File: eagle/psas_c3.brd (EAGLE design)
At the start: 100 x 80 mm, 56 parts, among them IC1 CP2102, U1 MIC5219 3.3V, Y1 32MHz

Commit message: GPIO connection
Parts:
- added TP6: (no value), psas_c3:1X01_ROUND
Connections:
- new net DIO2: JP6.17, TP6.1, U$1.51
- new net PTD4: JP6.16, JP7.1
- new net PTE2: JP6.5, U$1.49
- net PTE18: now also U$1.7
- net PTE19: now also U$1.8
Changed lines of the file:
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@@
 <element name="JP6" library="pinhead" package="2X09/90" value="" x="-54.61" y="-82.55"/>
 <element name="JP7" library="SparkFun-v5" package="1X02" value="" x="-67.31" y="-93.98"/>
+<element name="TP6" library="psas_c3" package="1X01_ROUND" value="" x="-72.39" y="-91.44">
+<attribute name="BOM" value="EXCLUDE" x="-72.39" y="-91.44" size="1.778" layer="27" display="off"/>
+</element>
 </elements>
 <signals>
@@
 <wire x1="-34.94" y1="22.995" x2="-56.91" y2="-20.82" width="0" layer="19" extent="1-1"/>
 </signal>
-<signal name="N$32">
-<contactref element="IC1" pad="24"/>
-<contactref element="U$1" pad="29"/>
-<wire x1="-20.405" y1="26.11" x2="-54.11" y2="-18.02" width="0" layer="19" extent="1-1"/>
-</signal>
-<signal name="N$33">
-<contactref element="IC1" pad="23"/>
-<contactref element="U$1" pad="28"/>
-<wire x1="-20.88" y1="26.585" x2="-53.61" y2="-18.02" width="0" layer="19" extent="1-1"/>
-</signal>
 <signal name="N$34">
 <contactref element="C20" pad="1"/>
@@
 <signal name="PTE18">
 <contactref element="JP6" pad="10"/>
+<contactref element="U$1" pad="7"/>
+<wire x1="-27.855" y1="22.61" x2="-54.61" y2="-86.36" width="0" layer="19" extent="1-1"/>
 </signal>
 <signal name="PTE17">
@@
 <signal name="PTE19">
 <contactref element="JP6" pad="11"/>
+<contactref element="U$1" pad="8"/>
+<wire x1="-27.855" y1="23.11" x2="-52.07" y2="-88.9" width="0" layer="19" extent="1-1"/>
+</signal>
+<signal name="PTE2">
+<contactref element="U$1" pad="49"/>
+<contactref element="JP6" pad="5"/>
+<wire x1="-23.88" y1="19.135" x2="-59.69" y2="-88.9" width="0" layer="19" extent="1-1"/>
+</signal>
+<signal name="DIO2">
+<contactref element="U$1" pad="51"/>
+<contactref element="JP6" pad="17"/>
+<contactref element="TP6" pad="1"/>
+<wire x1="-44.45" y1="-88.9" x2="-72.39" y2="-91.44" width="0" layer="19" extent="1-1"/>
+<wire x1="-24.88" y1="19.135" x2="-44.45" y2="-88.9" width="0" layer="19" extent="1-1"/>
+</signal>
+<signal name="PTD4">
+<contactref element="JP6" pad="16"/>
+<contactref element="JP7" pad="1"/>
+<wire x1="-46.99" y1="-86.36" x2="-67.31" y2="-93.98" width="0" layer="19" extent="1-1"/>
+</signal>
+<signal name="N$39">
+<contactref element="U$1" pad="29"/>
+<contactref element="IC1" pad="24"/>
+<wire x1="-20.405" y1="26.11" x2="-54.11" y2="-18.02" width="0" layer="19" extent="1-1"/>
+</signal>
+<signal name="N$32">
+<contactref element="U$1" pad="28"/>
+<contactref element="IC1" pad="23"/>
+<wire x1="-20.88" y1="26.585" x2="-53.61" y2="-18.02" width="0" layer="19" extent="1-1"/>
 </signal>
 </signals>

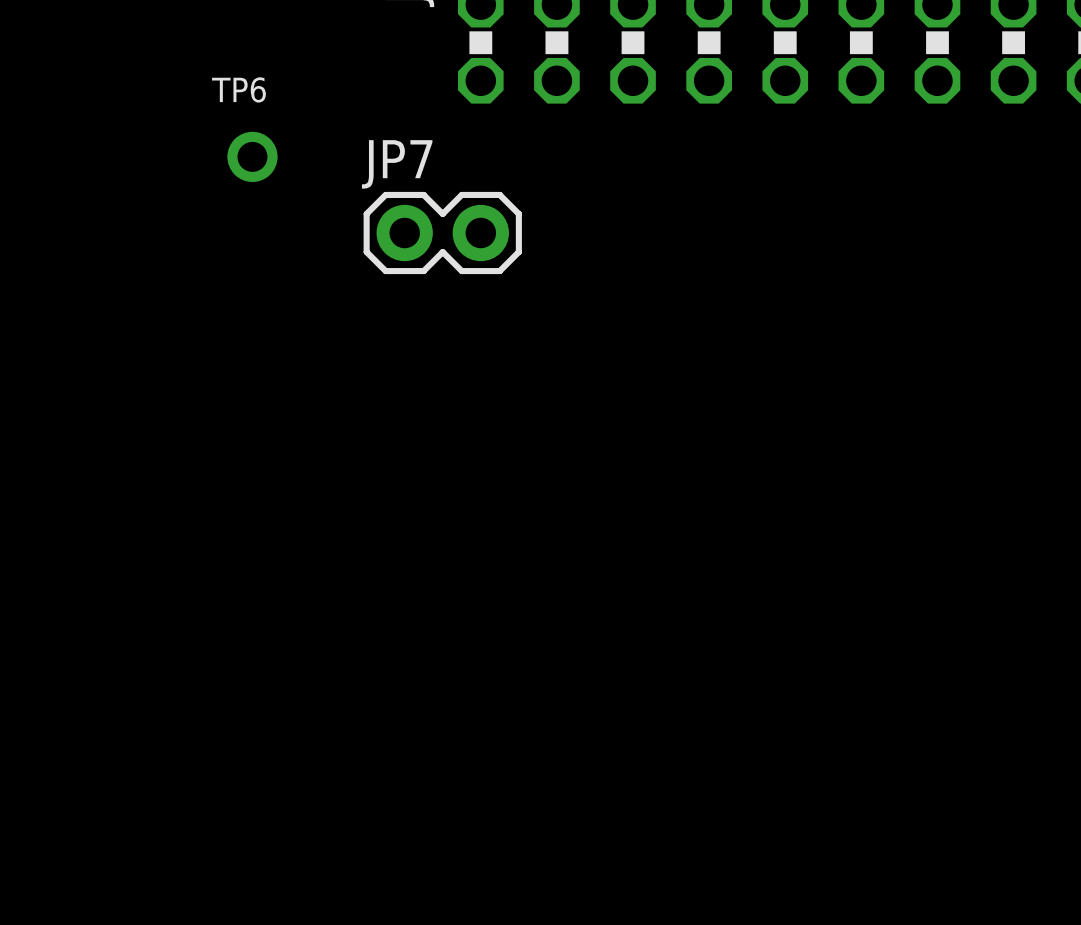
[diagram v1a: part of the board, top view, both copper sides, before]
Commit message: Added GPIO 2x9 pinheader
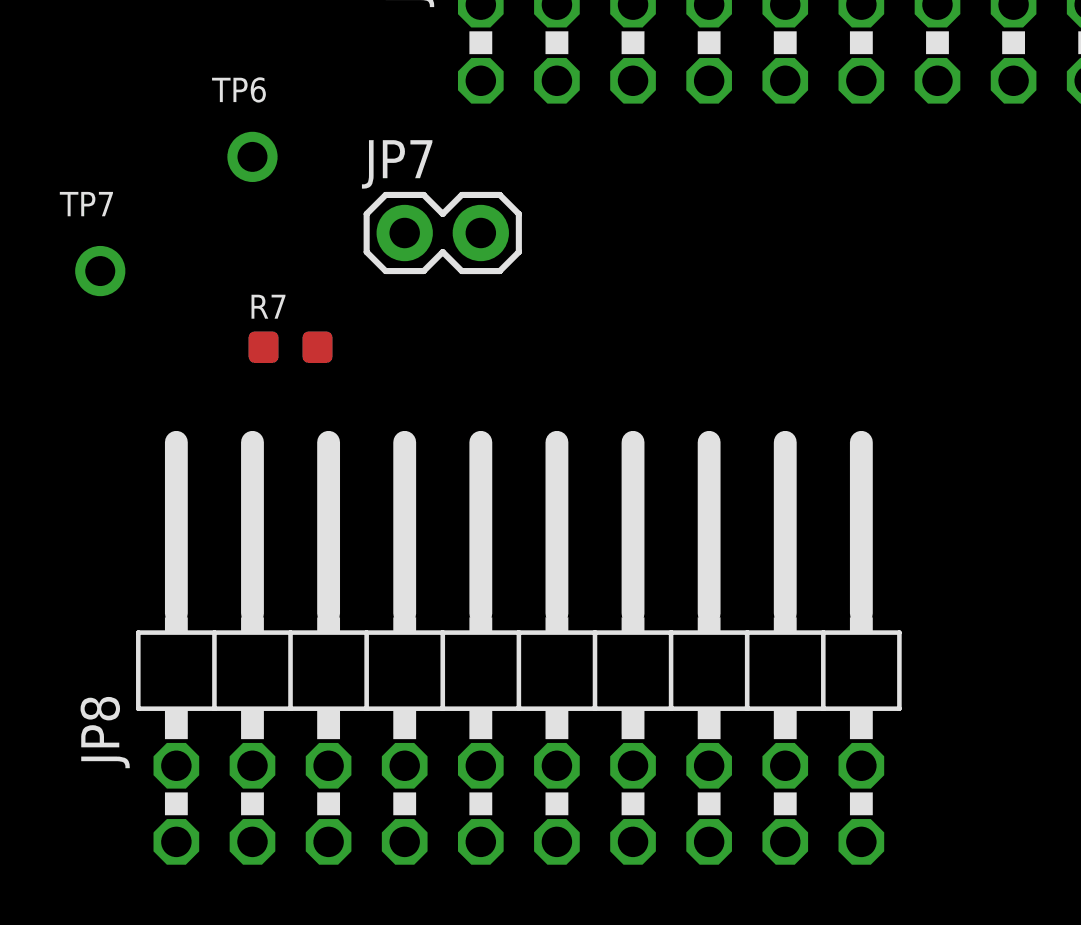
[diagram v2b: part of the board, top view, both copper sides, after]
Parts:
- added JP8: (no value), pinhead:2X10/90
- added R7: 0, rcl_custom:.0603-A-NOSILK
- added TP7: (no value), psas_c3:1X01_ROUND
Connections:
- net N$38 renamed DIO4
- new net DIO3: JP6.6, TP7.1, U$1.52
- new net N$40: JP6.3, R7.2
- new net N$41: JP2.1
- new net PTAG_19: R7.1, U$1.16
- new net PTC3: JP6.9, U$1.26
- new net PTC4: JP6.13, U$1.23
- new net V_BRD: JP6.1
- net GND: now also JP6.18, JP6.4
- net N$15: no longer JP2.1
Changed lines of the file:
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@@
 <attribute name="BOM" value="EXCLUDE" x="-72.39" y="-91.44" size="1.778" layer="27" display="off"/>
 </element>
+<element name="R7" library="rcl_custom" package=".0603-A-NOSILK" value="0" x="-71.12" y="-97.79"/>
+<element name="TP7" library="psas_c3" package="1X01_ROUND" value="" x="-77.47" y="-95.25">
+<attribute name="BOM" value="EXCLUDE" x="-77.47" y="-95.25" size="1.778" layer="27" display="off"/>
+</element>
+<element name="JP8" library="pinhead" package="2X10/90" value="" x="-63.5" y="-107.95"/>
 </elements>
 <signals>
@@
 <contactref element="JP5" pad="5"/>
 <contactref element="JP5" pad="3"/>
+<contactref element="JP6" pad="18"/>
+<contactref element="JP6" pad="4"/>
+<wire x1="-44.45" y1="-86.36" x2="-62.23" y2="-86.36" width="0" layer="19" extent="1-1"/>
+<wire x1="-67.31" y1="-63.5" x2="-62.23" y2="-86.36" width="0" layer="19" extent="1-1"/>
 <wire x1="-67.31" y1="-60.96" x2="-67.31" y2="-63.5" width="0" layer="19" extent="1-1"/>
 <wire x1="-55.08" y1="-54.61" x2="-67.31" y2="-60.96" width="0" layer="19" extent="1-1"/>
@@
 <wire x1="-20.405" y1="24.11" x2="-18.885" y2="28.23" width="0" layer="19" extent="1-1"/>
 </signal>
-<signal name="N$14">
-<contactref element="U$1" pad="54"/>
-<contactref element="JP2" pad="2"/>
-<wire x1="-35.56" y1="29.21" x2="-26.38" y2="19.135" width="0" layer="19" extent="1-1"/>
-</signal>
 <signal name="N$15">
 <contactref element="U$1" pad="15"/>
-<contactref element="JP2" pad="1"/>
-<wire x1="-27.38" y1="26.585" x2="-38.1" y2="29.21" width="0" layer="19" extent="1-1"/>
 </signal>
 <signal name="N$16">
@@
 <contactref element="JP5" pad="9"/>
 </signal>
-<signal name="N$38">
+<signal name="DIO4">
 <contactref element="U$1" pad="53"/>
 <contactref element="JP7" pad="2"/>
@@
 <wire x1="-20.88" y1="26.585" x2="-53.61" y2="-18.02" width="0" layer="19" extent="1-1"/>
 </signal>
+<signal name="V_BRD">
+<contactref element="JP6" pad="1"/>
+</signal>
+<signal name="PTAG_19">
+<contactref element="U$1" pad="16"/>
+<contactref element="R7" pad="1"/>
+<wire x1="-26.88" y1="26.585" x2="-72.02" y2="-97.79" width="0" layer="19" extent="1-1"/>
+</signal>
+<signal name="N$40">
+<contactref element="R7" pad="2"/>
+<contactref element="JP6" pad="3"/>
+<wire x1="-62.23" y1="-88.9" x2="-70.22" y2="-97.79" width="0" layer="19" extent="1-1"/>
+</signal>
+<signal name="N$14">
+<contactref element="U$1" pad="54"/>
+<contactref element="JP2" pad="2"/>
+<wire x1="-35.56" y1="29.21" x2="-26.38" y2="19.135" width="0" layer="19" extent="1-1"/>
+</signal>
+<signal name="N$41">
+<contactref element="JP2" pad="1"/>
+</signal>
+<signal name="DIO3">
+<contactref element="U$1" pad="52"/>
+<contactref element="JP6" pad="6"/>
+<contactref element="TP7" pad="1"/>
+<wire x1="-59.69" y1="-86.36" x2="-77.47" y2="-95.25" width="0" layer="19" extent="1-1"/>
+<wire x1="-25.38" y1="19.135" x2="-59.69" y2="-86.36" width="0" layer="19" extent="1-1"/>
+</signal>
+<signal name="PTC3">
+<contactref element="U$1" pad="26"/>
+<contactref element="JP6" pad="9"/>
+<wire x1="-21.88" y1="26.585" x2="-54.61" y2="-88.9" width="0" layer="19" extent="1-1"/>
+</signal>
+<signal name="PTC4">
+<contactref element="U$1" pad="23"/>
+<contactref element="JP6" pad="13"/>
+<wire x1="-23.38" y1="26.585" x2="-49.53" y2="-88.9" width="0" layer="19" extent="1-1"/>
+</signal>
 </signals>

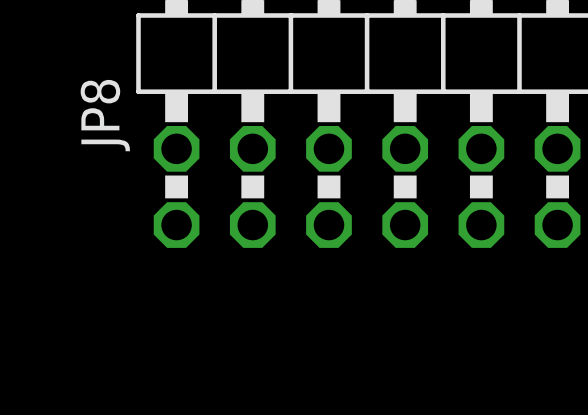
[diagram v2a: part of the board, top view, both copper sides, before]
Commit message: GPIO connection made
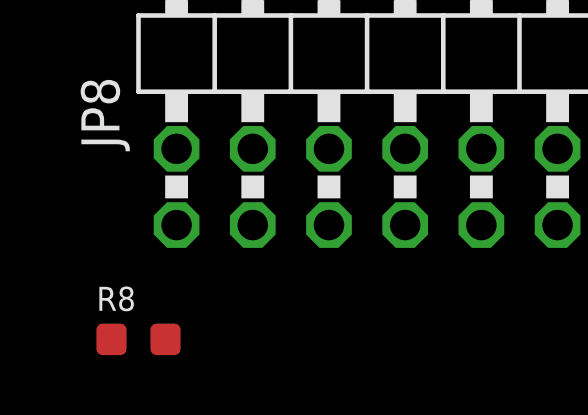
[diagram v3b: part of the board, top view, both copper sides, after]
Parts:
- added R8: 0, rcl_custom:.0603-A-NOSILK
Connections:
- net PTAG_19 renamed PTA19
- removed net N$13: R1.1, S2.A2, U$1.33
- removed net N$14: JP2.2, U$1.54
- removed net N$32: IC1.23, U$1.28
- removed net N$39: IC1.24, U$1.29
- removed net N$41: JP2.1
- removed net V_BRD: JP6.1
- new net DIO5: JP2.2, JP8.16, U$1.54
- new net PTA18: JP2.1, R8.2, U$1.15
- new net PTA20: JP8.10, R1.1, S2.A2, U$1.33
- new net PTA4: JP8.17, U$1.12
- new net PTB0: JP8.9, U$1.17
- new net PTB1: JP6.8, U$1.18
- new net PTB17: JP8.14, U$1.22
- new net PTB2: JP8.12, U$1.21
- new net PTC1: JP8.13, U$1.24
- new net PTC2: JP8.11, U$1.25
- new net PTD5: IC1.23, JP8.18, U$1.28
- new net PTD6: IC1.24, JP8.19, U$1.29
- new net PTD7: JP8.20, U$1.31
- net GND: now also JP8.15, JP8.3
- net N$15: now also JP6.2, R8.1; no longer U$1.15
- net V+: now also JP6.1, JP8.1
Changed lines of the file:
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@@
 </element>
 <element name="JP8" library="pinhead" package="2X10/90" value="" x="-63.5" y="-107.95"/>
+<element name="R8" library="rcl_custom" package=".0603-A-NOSILK" value="0" x="-76.2" y="-118.11"/>
 </elements>
 <signals>
@@
 <contactref element="JP6" pad="18"/>
 <contactref element="JP6" pad="4"/>
+<contactref element="JP8" pad="15"/>
+<contactref element="JP8" pad="3"/>
+<wire x1="-57.15" y1="-114.3" x2="-72.39" y2="-114.3" width="0" layer="19" extent="1-1"/>
+<wire x1="-62.23" y1="-86.36" x2="-57.15" y2="-114.3" width="0" layer="19" extent="1-1"/>
 <wire x1="-44.45" y1="-86.36" x2="-62.23" y2="-86.36" width="0" layer="19" extent="1-1"/>
 <wire x1="-67.31" y1="-63.5" x2="-62.23" y2="-86.36" width="0" layer="19" extent="1-1"/>
@@
 <contactref element="TP1" pad="1"/>
 <contactref element="C4" pad="1"/>
+<contactref element="JP6" pad="1"/>
+<contactref element="JP8" pad="1"/>
+<wire x1="-64.77" y1="-88.9" x2="-74.93" y2="-114.3" width="0" layer="19" extent="1-1"/>
+<wire x1="-39.1" y1="4.35" x2="-64.77" y2="-88.9" width="0" layer="19" extent="1-1"/>
 <wire x1="-46.99" y1="29.21" x2="-39.1" y2="4.35" width="0" layer="19" extent="1-1"/>
 <wire x1="-21.12" y1="46.99" x2="-46.99" y2="29.21" width="0" layer="19" extent="1-1"/>
@@
 <contactref element="Y1" pad="3"/>
 <wire x1="-22.88" y1="19.135" x2="-39.44" y2="46.99" width="0" layer="19" extent="1-1"/>
-</signal>
-<signal name="N$13">
-<contactref element="U$1" pad="33"/>
-<contactref element="R1" pad="1"/>
-<contactref element="S2" pad="A2"/>
-<wire x1="-18.885" y1="28.23" x2="-27.47" y2="50.8" width="0" layer="19" extent="1-1"/>
-<wire x1="-20.405" y1="24.11" x2="-18.885" y2="28.23" width="0" layer="19" extent="1-1"/>
-</signal>
-<signal name="N$15">
-<contactref element="U$1" pad="15"/>
 </signal>
 <signal name="N$16">
@@
 <contactref element="JP5" pad="9"/>
 </signal>
-<signal name="DIO4">
-<contactref element="U$1" pad="53"/>
-<contactref element="JP7" pad="2"/>
-<wire x1="-25.88" y1="19.135" x2="-64.77" y2="-93.98" width="0" layer="19" extent="1-1"/>
-</signal>
 <signal name="PTE0">
 <contactref element="U$1" pad="32"/>
@@
 </signal>
 <signal name="DIO2">
+<contactref element="JP6" pad="17"/>
 <contactref element="U$1" pad="51"/>
-<contactref element="JP6" pad="17"/>
 <contactref element="TP6" pad="1"/>
 <wire x1="-44.45" y1="-88.9" x2="-72.39" y2="-91.44" width="0" layer="19" extent="1-1"/>
@@
 <wire x1="-46.99" y1="-86.36" x2="-67.31" y2="-93.98" width="0" layer="19" extent="1-1"/>
 </signal>
-<signal name="N$39">
-<contactref element="U$1" pad="29"/>
-<contactref element="IC1" pad="24"/>
-<wire x1="-20.405" y1="26.11" x2="-54.11" y2="-18.02" width="0" layer="19" extent="1-1"/>
-</signal>
-<signal name="N$32">
-<contactref element="U$1" pad="28"/>
-<contactref element="IC1" pad="23"/>
-<wire x1="-20.88" y1="26.585" x2="-53.61" y2="-18.02" width="0" layer="19" extent="1-1"/>
-</signal>
-<signal name="V_BRD">
-<contactref element="JP6" pad="1"/>
-</signal>
-<signal name="PTAG_19">
-<contactref element="U$1" pad="16"/>
-<contactref element="R7" pad="1"/>
-<wire x1="-26.88" y1="26.585" x2="-72.02" y2="-97.79" width="0" layer="19" extent="1-1"/>
-</signal>
 <signal name="N$40">
 <contactref element="R7" pad="2"/>
@@
 <wire x1="-62.23" y1="-88.9" x2="-70.22" y2="-97.79" width="0" layer="19" extent="1-1"/>
 </signal>
-<signal name="N$14">
-<contactref element="U$1" pad="54"/>
-<contactref element="JP2" pad="2"/>
-<wire x1="-35.56" y1="29.21" x2="-26.38" y2="19.135" width="0" layer="19" extent="1-1"/>
-</signal>
-<signal name="N$41">
+<signal name="PTA18">
 <contactref element="JP2" pad="1"/>
+<contactref element="U$1" pad="15"/>
+<contactref element="R8" pad="2"/>
+<wire x1="-38.1" y1="29.21" x2="-75.3" y2="-118.11" width="0" layer="19" extent="1-1"/>
+<wire x1="-27.38" y1="26.585" x2="-38.1" y2="29.21" width="0" layer="19" extent="1-1"/>
 </signal>
 <signal name="DIO3">
@@
 <wire x1="-23.38" y1="26.585" x2="-49.53" y2="-88.9" width="0" layer="19" extent="1-1"/>
 </signal>
+<signal name="PTB0">
+<contactref element="U$1" pad="17"/>
+<contactref element="JP8" pad="9"/>
+<wire x1="-26.38" y1="26.585" x2="-64.77" y2="-114.3" width="0" layer="19" extent="1-1"/>
+</signal>
+<signal name="PTB2">
+<contactref element="U$1" pad="21"/>
+<contactref element="JP8" pad="12"/>
+<wire x1="-24.38" y1="26.585" x2="-62.23" y2="-111.76" width="0" layer="19" extent="1-1"/>
+</signal>
+<signal name="PTB17">
+<contactref element="U$1" pad="22"/>
+<contactref element="JP8" pad="14"/>
+<wire x1="-23.88" y1="26.585" x2="-59.69" y2="-111.76" width="0" layer="19" extent="1-1"/>
+</signal>
+<signal name="PTC1">
+<contactref element="U$1" pad="24"/>
+<contactref element="JP8" pad="13"/>
+<wire x1="-22.88" y1="26.585" x2="-59.69" y2="-114.3" width="0" layer="19" extent="1-1"/>
+</signal>
+<signal name="PTC2">
+<contactref element="U$1" pad="25"/>
+<contactref element="JP8" pad="11"/>
+<wire x1="-22.38" y1="26.585" x2="-62.23" y2="-114.3" width="0" layer="19" extent="1-1"/>
+</signal>
+<signal name="PTD5">
+<contactref element="U$1" pad="28"/>
+<contactref element="IC1" pad="23"/>
+<contactref element="JP8" pad="18"/>
+<wire x1="-53.61" y1="-18.02" x2="-54.61" y2="-111.76" width="0" layer="19" extent="1-1"/>
+<wire x1="-20.88" y1="26.585" x2="-53.61" y2="-18.02" width="0" layer="19" extent="1-1"/>
+</signal>
+<signal name="PTD6">
+<contactref element="U$1" pad="29"/>
+<contactref element="IC1" pad="24"/>
+<contactref element="JP8" pad="19"/>
+<wire x1="-54.11" y1="-18.02" x2="-52.07" y2="-114.3" width="0" layer="19" extent="1-1"/>
+<wire x1="-20.405" y1="26.11" x2="-54.11" y2="-18.02" width="0" layer="19" extent="1-1"/>
+</signal>
+<signal name="PTD7">
+<contactref element="U$1" pad="31"/>
+<contactref element="JP8" pad="20"/>
+<wire x1="-20.405" y1="25.11" x2="-52.07" y2="-111.76" width="0" layer="19" extent="1-1"/>
+</signal>
+<signal name="N$15">
+<contactref element="JP6" pad="2"/>
+<contactref element="R8" pad="1"/>
+<wire x1="-64.77" y1="-86.36" x2="-77.1" y2="-118.11" width="0" layer="19" extent="1-1"/>
+</signal>
+<signal name="PTB1">
+<contactref element="U$1" pad="18"/>
+<contactref element="JP6" pad="8"/>
+<wire x1="-25.88" y1="26.585" x2="-57.15" y2="-86.36" width="0" layer="19" extent="1-1"/>
+</signal>
+<signal name="PTA4">
+<contactref element="JP8" pad="17"/>
+<contactref element="U$1" pad="12"/>
+<wire x1="-27.855" y1="25.11" x2="-54.61" y2="-114.3" width="0" layer="19" extent="1-1"/>
+</signal>
+<signal name="PTA19">
+<contactref element="U$1" pad="16"/>
+<contactref element="R7" pad="1"/>
+<wire x1="-26.88" y1="26.585" x2="-72.02" y2="-97.79" width="0" layer="19" extent="1-1"/>
+</signal>
+<signal name="PTA20">
+<contactref element="U$1" pad="33"/>
+<contactref element="R1" pad="1"/>
+<contactref element="S2" pad="A2"/>
+<contactref element="JP8" pad="10"/>
+<wire x1="-20.405" y1="24.11" x2="-64.77" y2="-111.76" width="0" layer="19" extent="1-1"/>
+<wire x1="-18.885" y1="28.23" x2="-20.405" y2="24.11" width="0" layer="19" extent="1-1"/>
+<wire x1="-27.47" y1="50.8" x2="-18.885" y2="28.23" width="0" layer="19" extent="1-1"/>
+</signal>
+<signal name="DIO4">
+<contactref element="U$1" pad="53"/>
+<contactref element="JP7" pad="2"/>
+<wire x1="-25.88" y1="19.135" x2="-64.77" y2="-93.98" width="0" layer="19" extent="1-1"/>
+</signal>
+<signal name="DIO5">
+<contactref element="U$1" pad="54"/>
+<contactref element="JP2" pad="2"/>
+<contactref element="JP8" pad="16"/>
+<wire x1="-26.38" y1="19.135" x2="-57.15" y2="-111.76" width="0" layer="19" extent="1-1"/>
+<wire x1="-35.56" y1="29.21" x2="-26.38" y2="19.135" width="0" layer="19" extent="1-1"/>
+</signal>
 </signals>
